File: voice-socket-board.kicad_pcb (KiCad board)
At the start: 2 copper layers, 150 x 100 mm, 280 parts, among them J1 JACK_MONO_SW, J2 JACK_MONO_SW, J3 JACK_MONO_SW, P1 CONN_01X03, P2 CONN_01X03, P3 CONN_02X05, P4 DDR3-DIMM, Q1 MMBT3904, Q10 2N3906, Q2 DMMT3904W, Q3 2N7002, Q4 2N7002, Q5 MMBT3904, Q6 2N3906, Q7 MMBT3904, Q8 MMBT3904, Q9 MMBT3904, SW1 SPST, SW10 SP3T, SW11 SP3T, SW12 SP3T, SW13 SP3T, SW14 SPST, SW15 TACT_SWITCH, SW2 SPST, SW3 SP3T, SW4 SP3T, SW5 SPST, SW6 SPST, SW7 Switch_SPDT_x2, SW8 2P3T, SW9 SP3T, U1 LM833, U10 TL072-, U11 NE5534, U2 TL072-, U3 TL072-, U4 TL072-, U5 TL072-, U6 TL072-, U7 MAX9945, U8 CD4013, U9 TL072-

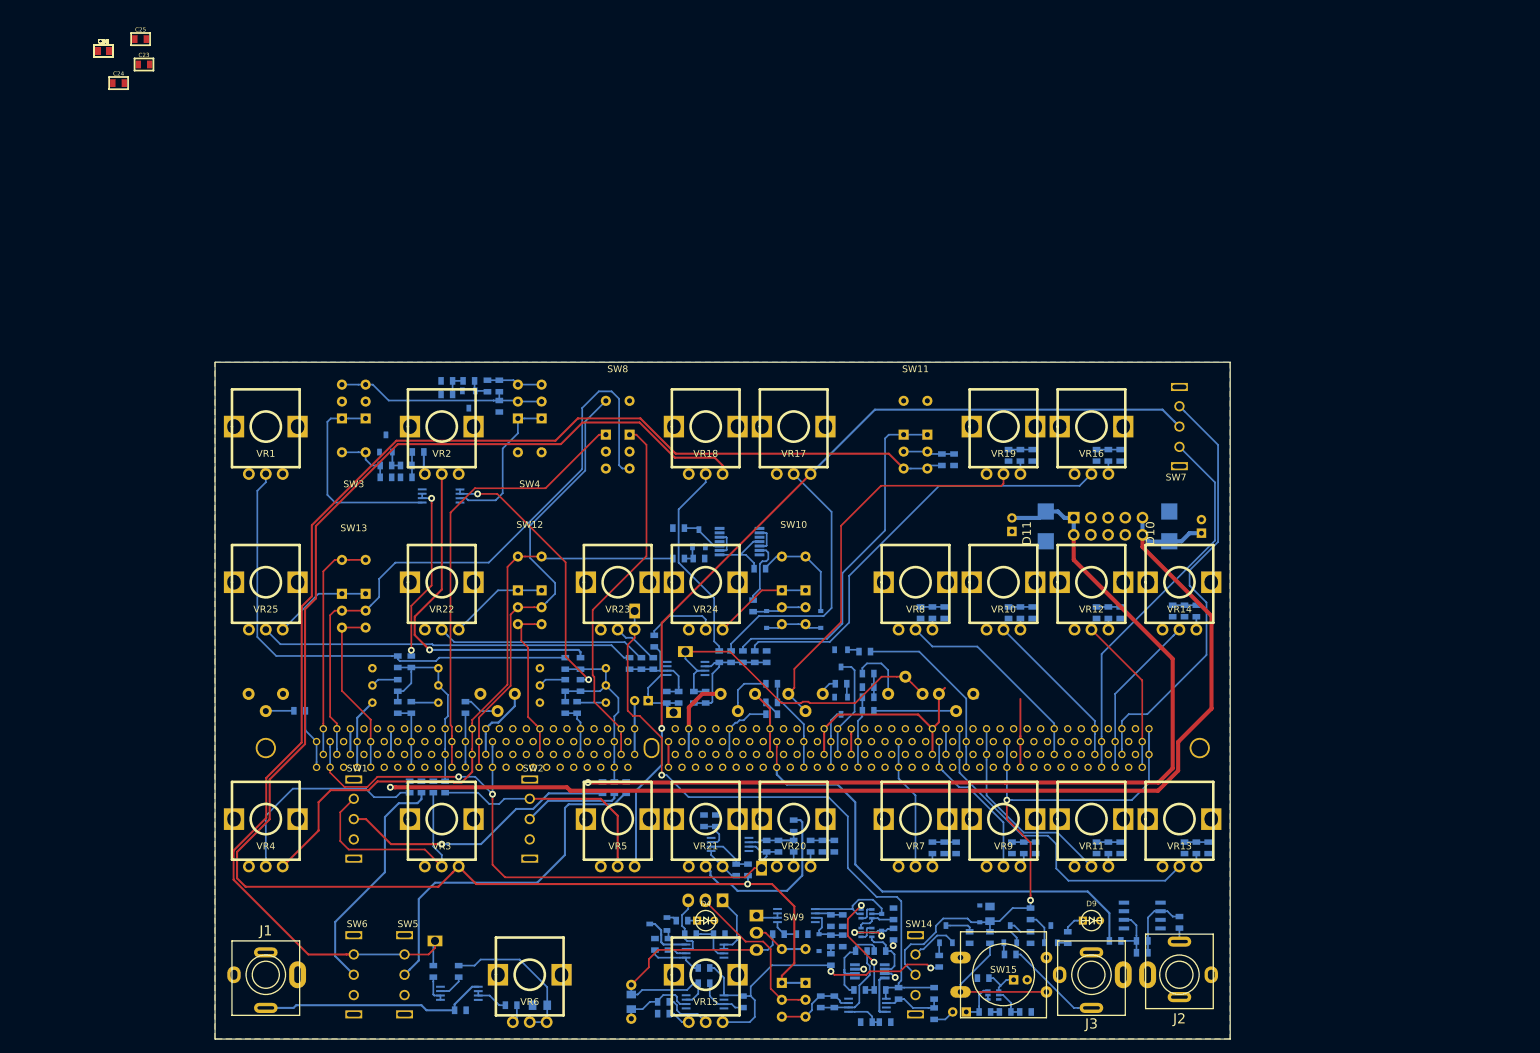
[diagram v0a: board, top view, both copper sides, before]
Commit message: power routed. now placing and routing decoupling caps
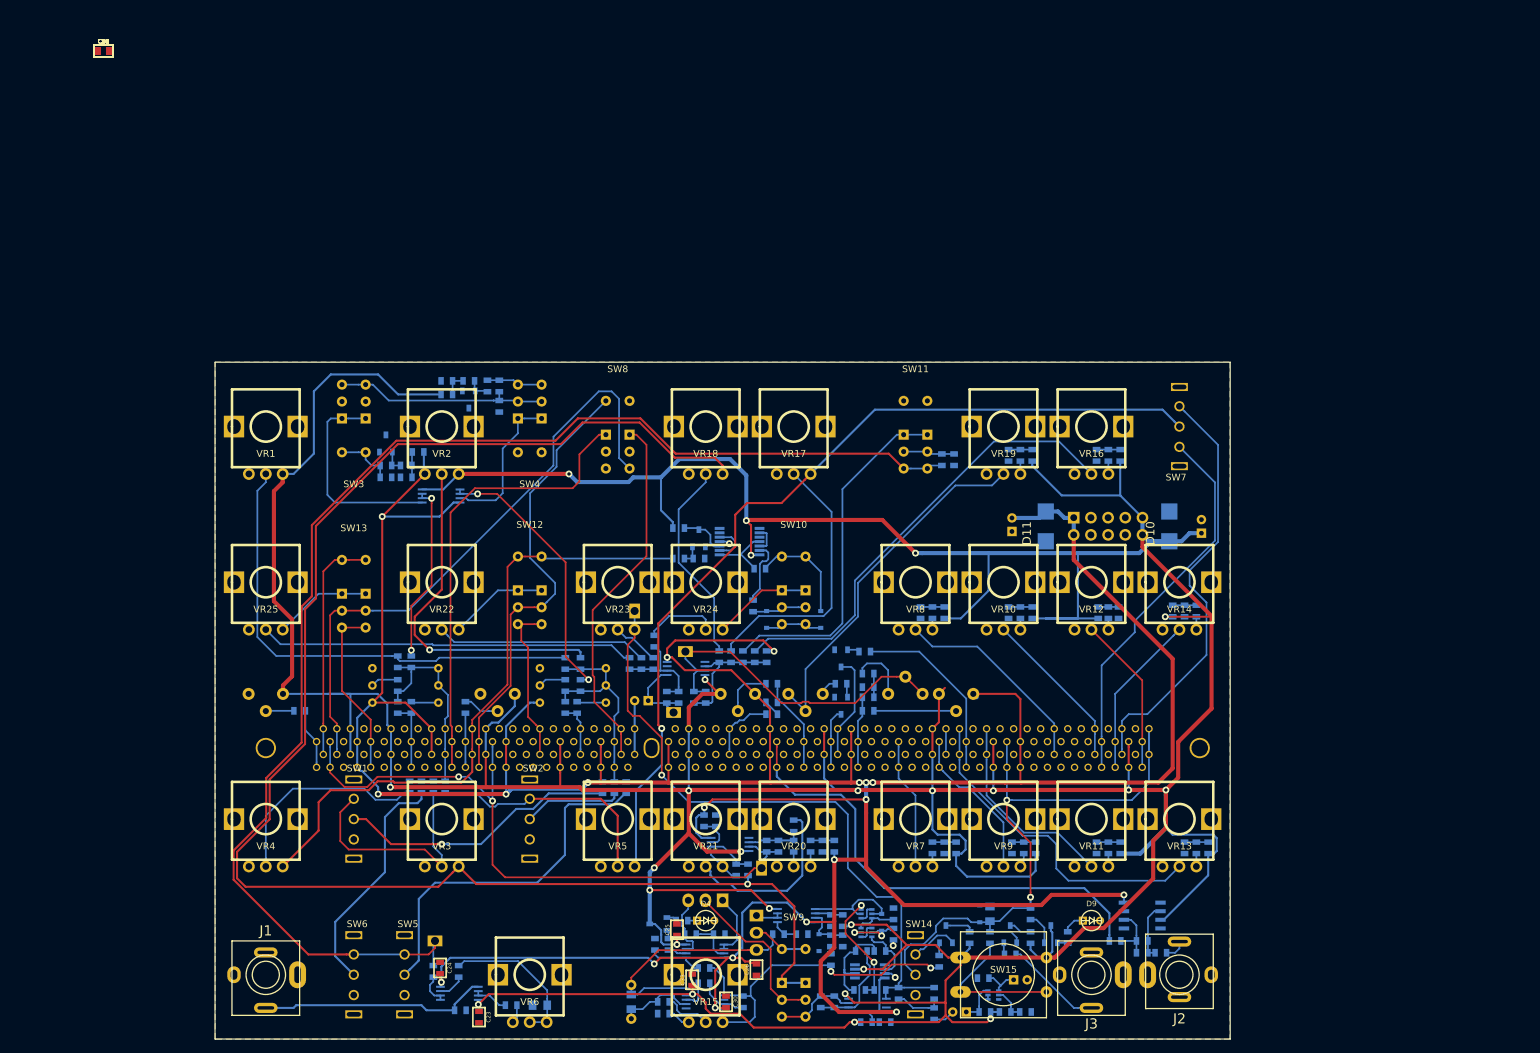
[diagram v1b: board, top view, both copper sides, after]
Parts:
- moved C30 167.9 mm to (120.5, 134.5), turned to 270 degrees
- moved C26 166.6 mm to (125.0, 129.8), turned to 90 degrees
- moved C33 162.5 mm to (115.5, 131.2), turned to 90 degrees
- moved C25 153.6 mm to (113.2, 123.9), turned to 90 degrees
- moved C23 149.2 mm to (84.0, 136.8), turned to 270 degrees
- moved C24 139.1 mm to (78.2, 129.5), turned to 270 degrees
- moved R123 5.27 mm to (184.8, 127.2), turned to 180 degrees
- moved C11 3.25 mm to (178.5, 77.0)
- moved R42 3.25 mm to (175.5, 77.0)
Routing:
- net +12V: track 246.2 -> 914.2 mm, vias 2 -> 25
- net -12V: track 189.0 -> 585.9 mm, vias 1 -> 19
- net Net-(TR1-Pad1): track 59.7 -> 53.9 mm
- net VCO1_PULSE: track 96.3 -> 91.3 mm
- net EG2_OUT: track 128.3 -> 131.7 mm
- net Net-(R97-Pad2): track 65.1 -> 67.6 mm
- net VCO1_SYNC_IN: track 65.4 -> 67.8 mm
- net Net-(C62-Pad2): track 10.6 -> 8.49 mm
- net Net-(U8-Pad2): track 3.97 -> 5.86 mm
- net GND: track 2.66 -> 4.23 mm, vias 2 -> 3
- net Net-(J2-Pad3): track 2.00 -> 3.17 mm
- net Net-(R98-Pad2): track 53.2 -> 52.1 mm
- net VCA_OUT: track 72.0 -> 71.1 mm
- net Net-(Q5-Pad3): track 6.38 -> 7.07 mm
- net Net-(C14-Pad2): track 41.4 -> 41.9 mm
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
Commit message: placing and routing decoupling caps
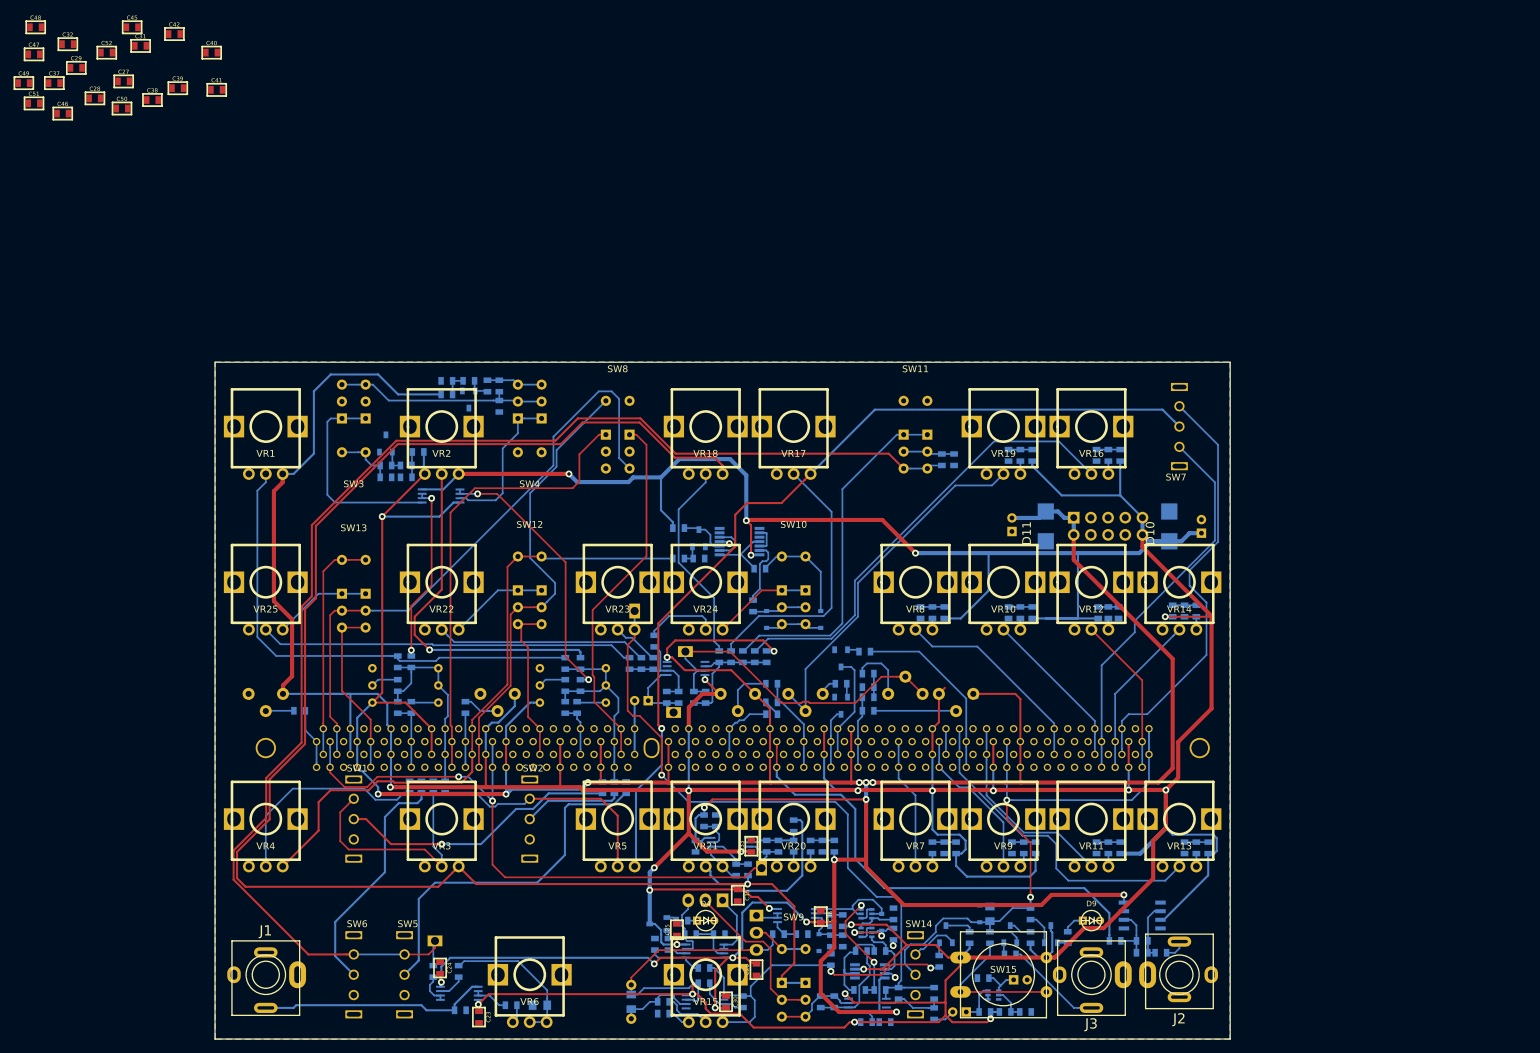
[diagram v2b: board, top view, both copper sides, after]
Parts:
- C34: moved to B.Cu
- moved C36 166.1 mm to (134.5, 121.9), turned to 270 degrees
- moved C35 156.0 mm to (122.2, 118.8), turned to 270 degrees
- moved C34 146.5 mm to (116.0, 111.5), turned to 90 degrees
- moved C33 21.6 mm to (124.2, 111.5)
- moved C41 17.7 mm to (45.2, -0.25)
- moved C40 16.0 mm to (44.5, -5.75)
- moved C51 12.8 mm to (18.2, 1.75)
- moved C49 12.7 mm to (16.8, -1.25)
- moved C39 12.3 mm to (39.5, -0.50)
- moved C46 11.0 mm to (22.5, 3.25)
- moved C42 10.8 mm to (39.0, -8.50)
- moved C48 10.6 mm to (18.5, -9.50)
- moved C47 10.3 mm to (18.2, -5.50)
- moved C38 10.2 mm to (35.8, 1.25)
- moved C50 8.93 mm to (31.2, 2.50)
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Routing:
- net +12V: track 914.2 -> 915.9 mm
- net -12V: track 585.9 -> 587.2 mm

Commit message: updating 3D models in library. Kicad 4.0 doesn't seem to like VRML1.0 format 3D models
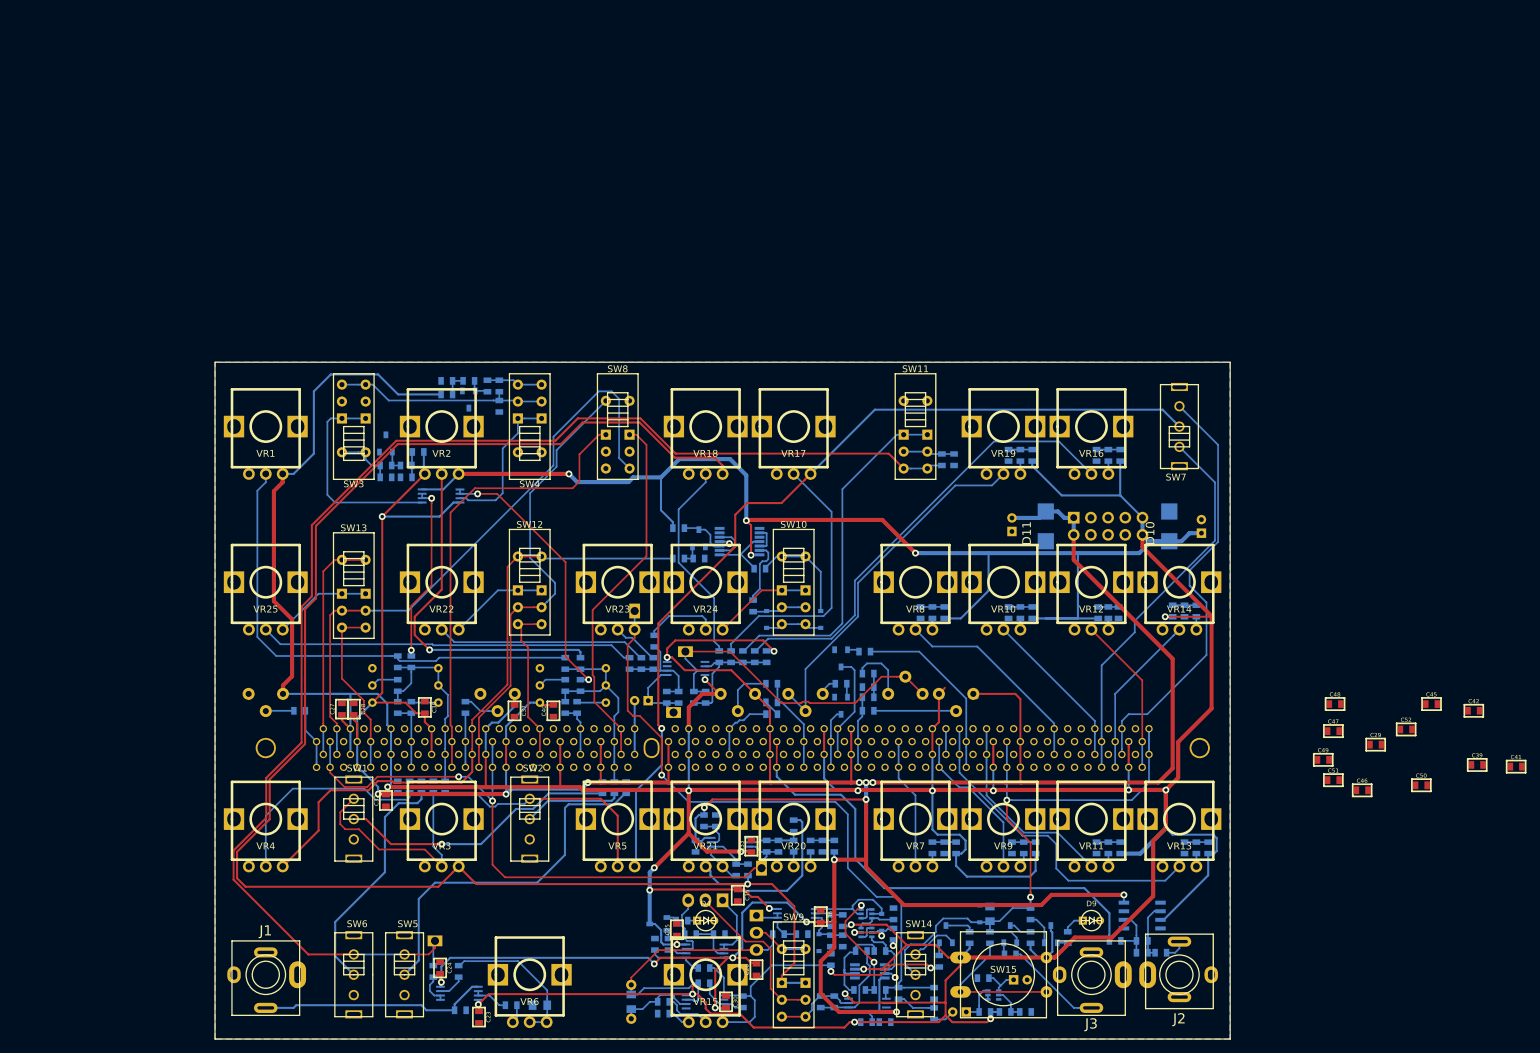
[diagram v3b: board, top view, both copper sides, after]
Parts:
- C31: moved to B.Cu
- moved C29 216.5 mm to (216.5, 96.5)
- moved C39 216.5 mm to (231.5, 99.5)
- moved C41 216.5 mm to (237.2, 99.8)
- moved C42 216.5 mm to (231.0, 91.5)
- moved C45 216.5 mm to (224.8, 90.5)
- moved C46 216.5 mm to (214.5, 103.2)
- moved C47 216.5 mm to (210.2, 94.5)
- moved C48 216.5 mm to (210.5, 90.5)
- moved C49 216.5 mm to (208.8, 98.8)
- moved C50 216.5 mm to (223.2, 102.5)
- moved C51 216.5 mm to (210.2, 101.8)
- moved C52 216.5 mm to (221.0, 94.2)
- moved C32 121.2 mm to (70.2, 104.8), turned to 90 degrees
- moved C31 115.9 mm to (72.0, 102.8), turned to 270 degrees
- moved C37 115.0 mm to (89.2, 91.5), turned to 270 degrees
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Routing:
- net -12V: track 587.2 -> 595.6 mm
- net +12V: track 915.9 -> 922.2 mm
- net LFO_MOD: track 35.0 -> 33.6 mm

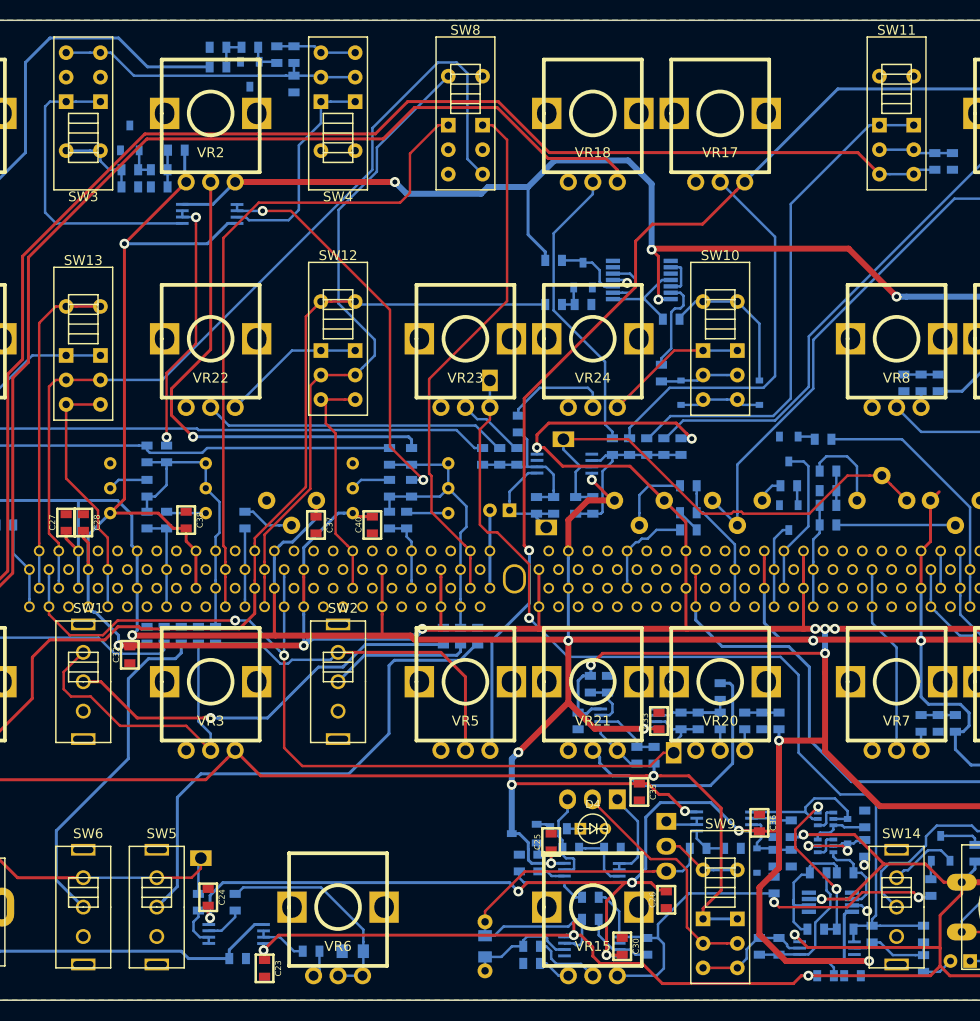
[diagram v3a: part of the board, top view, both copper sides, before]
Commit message: more updating 3D models. About to move ENV2 polarity switch to make more room for cutoff knob
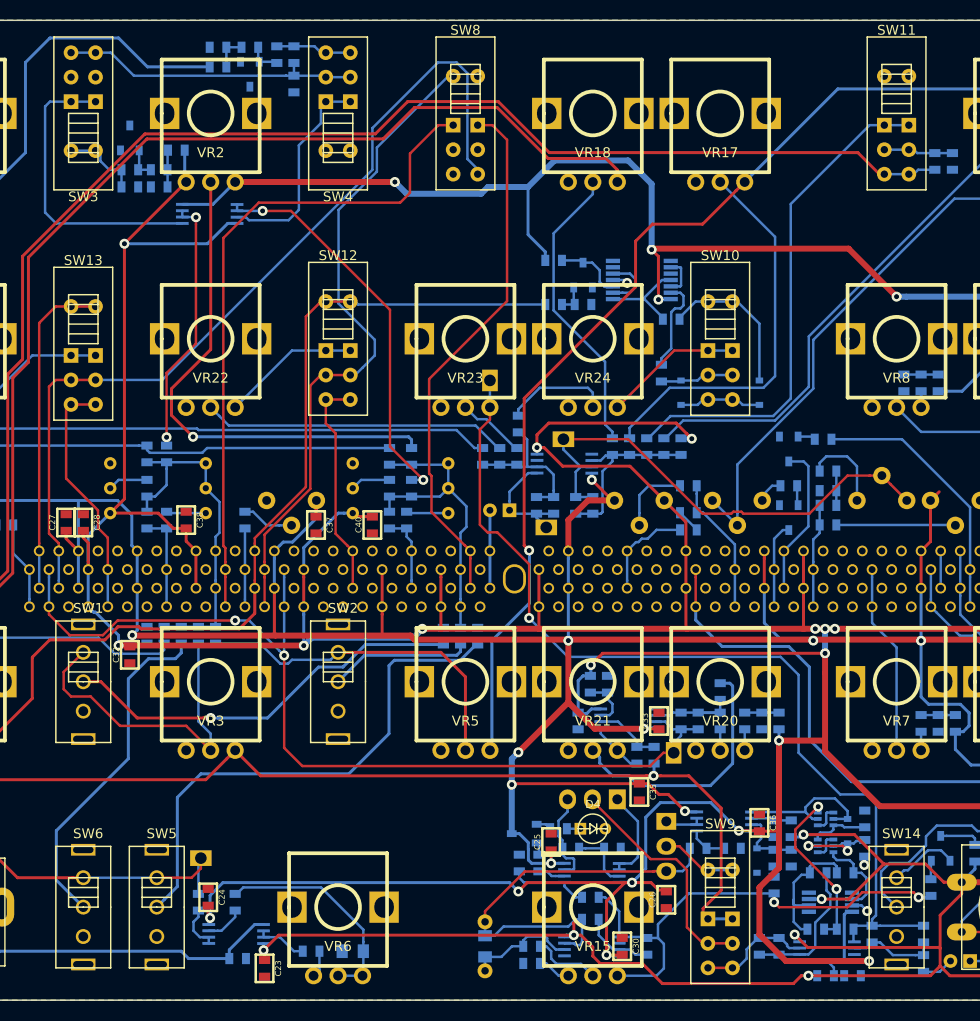
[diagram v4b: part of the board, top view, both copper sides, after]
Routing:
- net VCO1_PULSE: track 91.3 -> 27.6 mm
- net VCO1_SYNC_IN: track 67.8 -> 117.1 mm
- net VCO2_SYNC_IN: track 53.9 -> 68.3 mm

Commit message: more 3D model updating for modules
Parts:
- moved SW7 38.0 mm to (187.5, 87.5), turned to 270 degrees
- moved C55 13.0 mm to (188.2, 53.8)
- moved R95 13.0 mm to (191.8, 53.8)
- moved R96 13.0 mm to (190.0, 53.8)
- moved VR16 13.0 mm to (187.5, 49.5)
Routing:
- net EG2_ENV_OUT: track 63.4 -> 13.8 mm
- net EG2_INV_OUT: track 56.5 -> 26.1 mm
- net EG2_OUT: track 131.7 -> 155.8 mm
- net Net-(R97-Pad2): track 67.6 -> 80.6 mm
- net +12V: track 922.2 -> 927.9 mm
- net EG2_RELEASE_CV: track 24.3 -> 28.1 mm
- net -12V: track 595.6 -> 594.4 mm
